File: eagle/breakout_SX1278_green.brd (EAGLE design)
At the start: 28.6 x 28.6 mm, 20 parts, among them X1 734120110

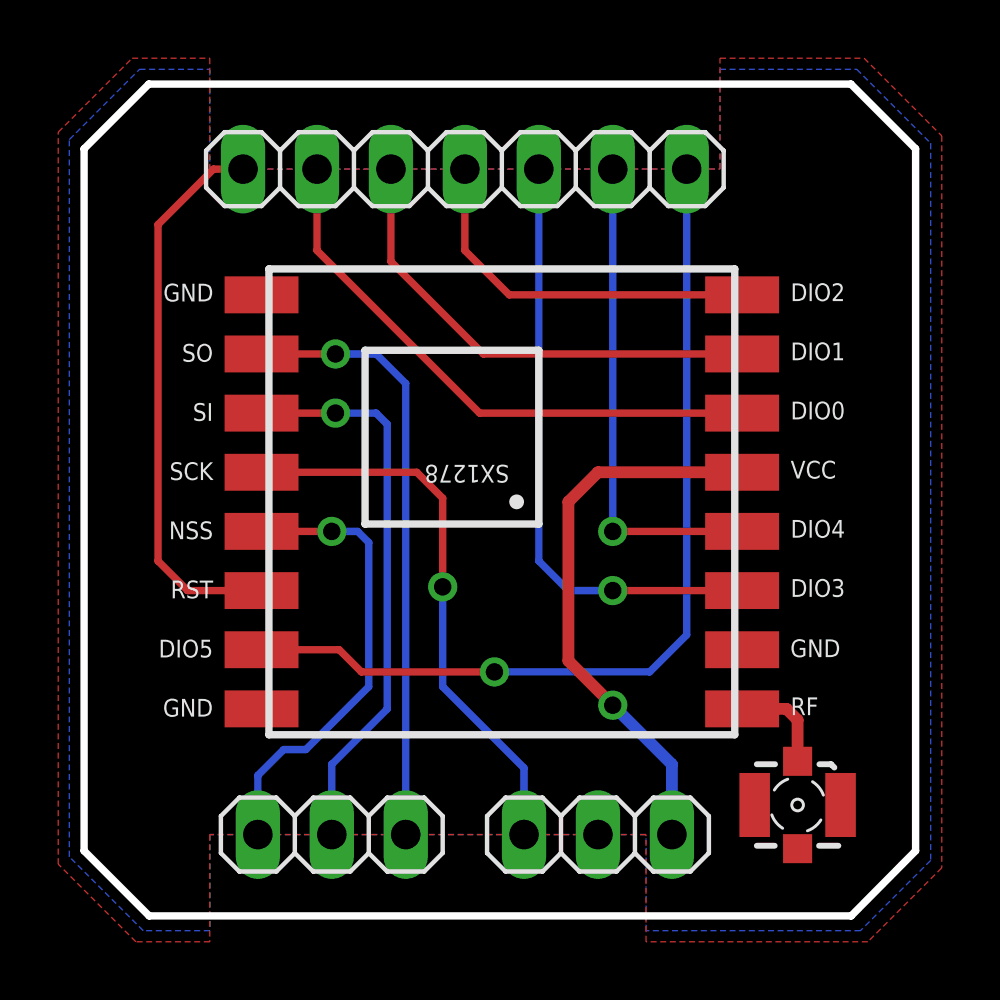
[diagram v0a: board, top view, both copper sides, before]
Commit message: Module layout update
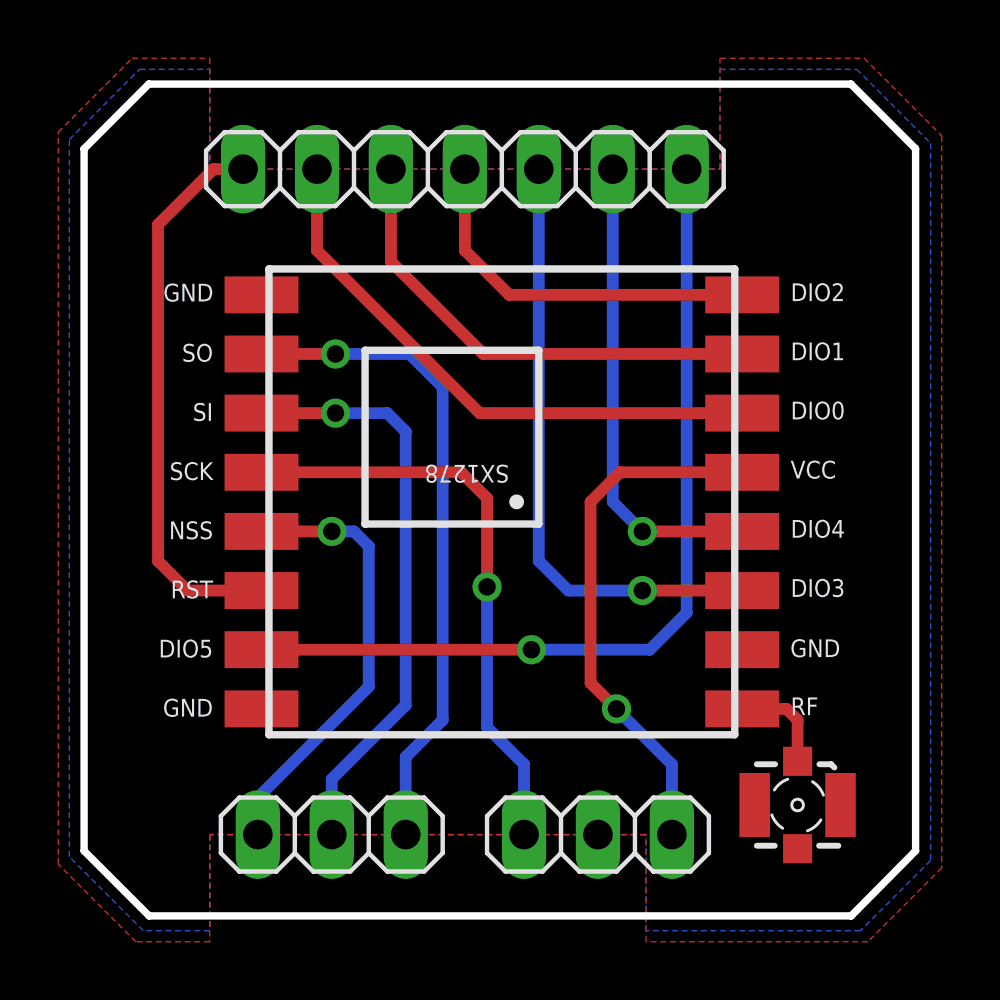
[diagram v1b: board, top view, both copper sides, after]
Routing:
- net MISO: track 20.9 -> 22.6 mm
- net 3.3V: track 19.3 -> 18.2 mm
- net DIO5: track 31.4 -> 30.4 mm
- net SCK: track 19.3 -> 20.2 mm
- net MOSI: track 19.4 -> 20.1 mm
- net DIO4: track 16.9 -> 16.3 mm
- net NSS: track 15.9 -> 15.4 mm
